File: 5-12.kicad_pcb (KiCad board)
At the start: 2 copper layers, 266.7 x 95.2 mm, 136 parts, among them SW1 SW_Push, U1 ATmega32U4-AU, Y1 16MHz

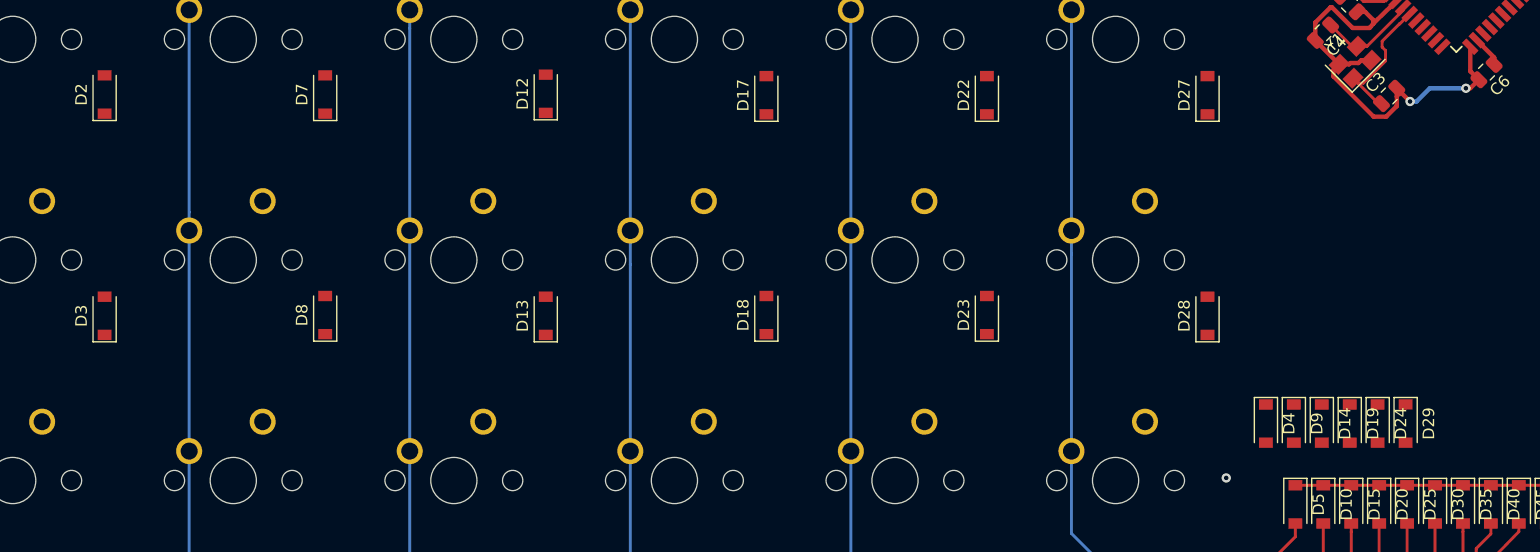
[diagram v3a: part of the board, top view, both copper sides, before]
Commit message: Moved left side of R2 into bank, did partial routing from bank back to switches to test the fit
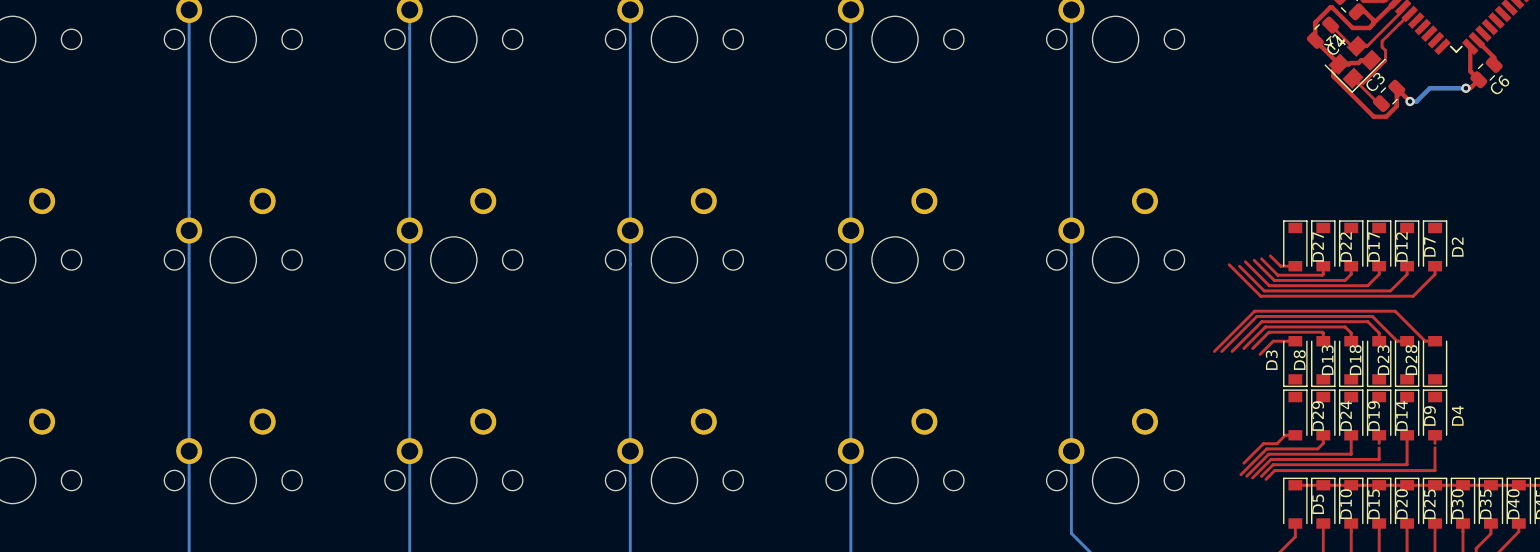
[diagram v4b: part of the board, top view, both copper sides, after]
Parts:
- moved D2 115.7 mm to (144.3, 115.6), turned to 270 degrees
- moved D3 102.9 mm to (132.2, 125.3)
- moved D7 94.4 mm to (141.9, 115.6), turned to 270 degrees
- moved D8 86.3 mm to (134.6, 125.3)
- moved D12 73.2 mm to (139.4, 115.6), turned to 270 degrees
- moved D13 69.7 mm to (137.0, 125.3)
- moved D18 53.1 mm to (139.4, 125.3)
- moved D17 52.2 mm to (137.0, 115.6), turned to 270 degrees
- moved D23 36.5 mm to (141.9, 125.3)
- moved D22 31.9 mm to (134.6, 115.6), turned to 270 degrees
- moved D28 20.0 mm to (144.3, 125.3)
- moved D27 15.2 mm to (132.2, 115.6), turned to 270 degrees
- moved D4 14.6 mm to (144.3, 130.2)
- moved D9 9.80 mm to (141.9, 130.2)
- moved D29 9.55 mm to (132.2, 130.2)
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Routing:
- net Net-(D28-Pad2): track 0.00 -> 21.6 mm
- net Net-(D2-Pad2): track 0.00 -> 20.4 mm
- net Net-(D23-Pad2): track 0.00 -> 18.1 mm
- net Net-(D4-Pad2): track 0.00 -> 17.6 mm
- net Net-(D7-Pad2): track 0.00 -> 16.7 mm
- net Net-(D9-Pad2): track 0.00 -> 15.2 mm
- net Net-(D18-Pad2): track 0.00 -> 14.9 mm
- net Net-(D12-Pad2): track 0.00 -> 13.5 mm
- net Net-(D14-Pad2): track 0.00 -> 13.3 mm
- net Net-(D19-Pad2): track 0.00 -> 11.4 mm
- net Net-(D13-Pad2): track 0.00 -> 11.0 mm
- net Net-(D17-Pad2): track 0.00 -> 10.0 mm
- net Net-(D24-Pad2): track 0.00 -> 8.93 mm
- net Net-(D8-Pad2): track 0.00 -> 7.41 mm
- net Net-(D22-Pad2): track 0.00 -> 6.65 mm
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
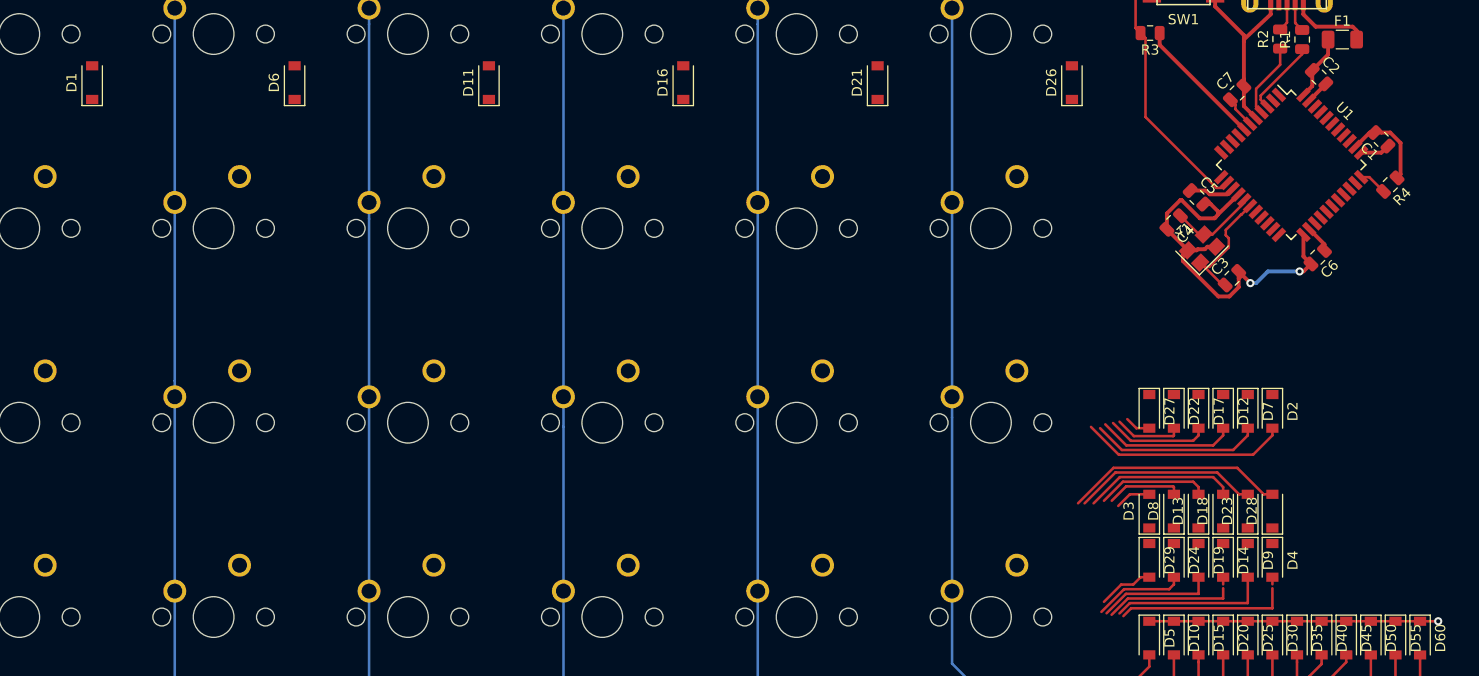
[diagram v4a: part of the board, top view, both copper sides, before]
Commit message: finished left diode banks and their initial routes
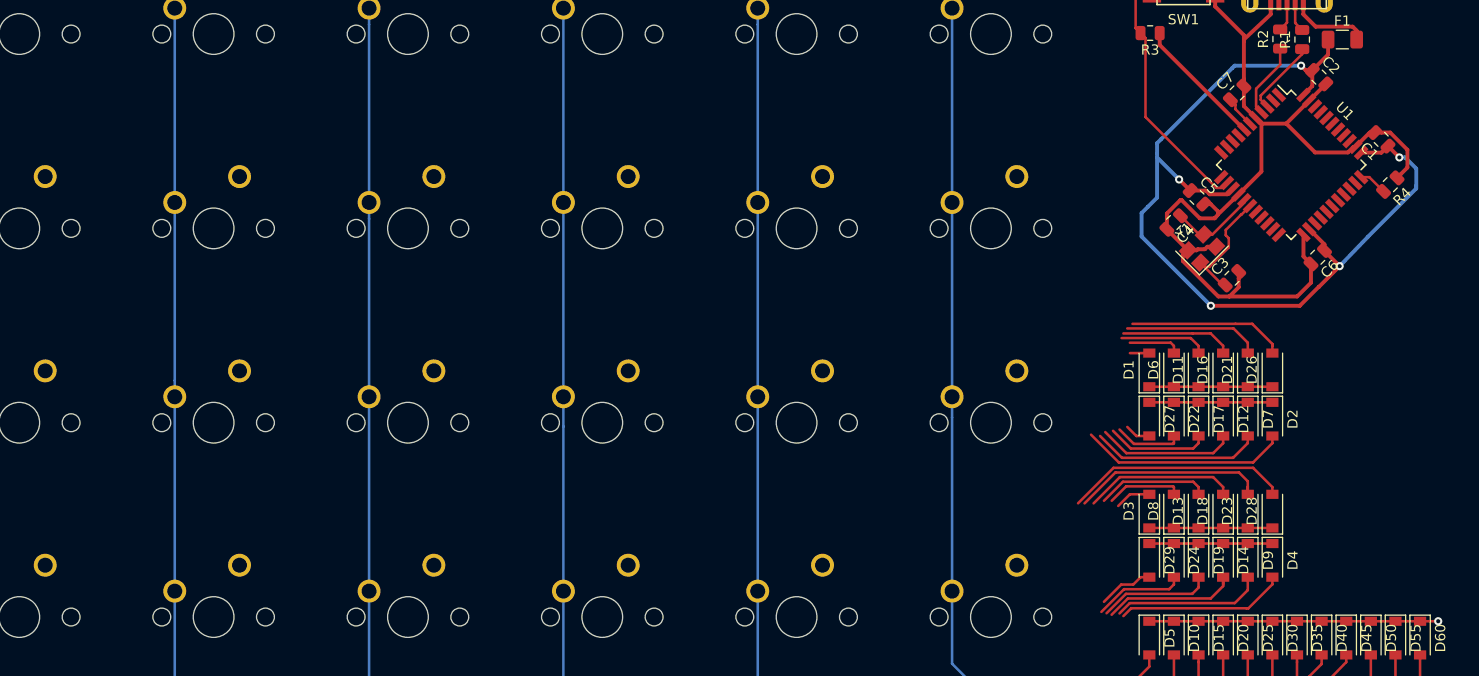
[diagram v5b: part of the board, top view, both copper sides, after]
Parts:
- moved D1 107.4 mm to (132.2, 111.5)
- moved D6 90.7 mm to (134.6, 111.5)
- moved D11 75.0 mm to (137.0, 111.5)
- moved D16 60.0 mm to (139.4, 111.5)
- moved D21 45.9 mm to (141.9, 111.5)
- moved D26 34.3 mm to (144.3, 111.5)
- moved D12 0.76 mm to (139.4, 116.3)
- moved D17 0.76 mm to (137.0, 116.3)
- moved D2 0.76 mm to (144.3, 116.3)
- moved D22 0.76 mm to (134.6, 116.3)
- moved D27 0.76 mm to (132.2, 116.3)
- moved D7 0.76 mm to (141.9, 116.3)
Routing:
- net +5V: track 29.5 -> 104.8 mm, vias 0 -> 5
- net GND: track 71.2 -> 96.7 mm, vias 2 -> 0
- net Net-(D26-Pad2): track 0.00 -> 15.4 mm
- net Net-(D21-Pad2): track 0.00 -> 13.4 mm
- net Row3: track 0.00 -> 12.1 mm
- net Row1: track 0.00 -> 12.1 mm
- net Row2: track 0.00 -> 12.1 mm
- net Row0: track 0.00 -> 12.1 mm
- net Net-(D16-Pad2): track 0.00 -> 11.0 mm
- net Net-(D11-Pad2): track 0.00 -> 8.57 mm
- net Net-(D6-Pad2): track 0.00 -> 5.15 mm
- net Net-(D1-Pad2): track 0.00 -> 1.90 mm
- net Net-(D23-Pad2): track 18.1 -> 19.1 mm
- net Net-(D4-Pad2): track 17.6 -> 16.6 mm
- net Net-(D9-Pad2): track 15.2 -> 14.4 mm

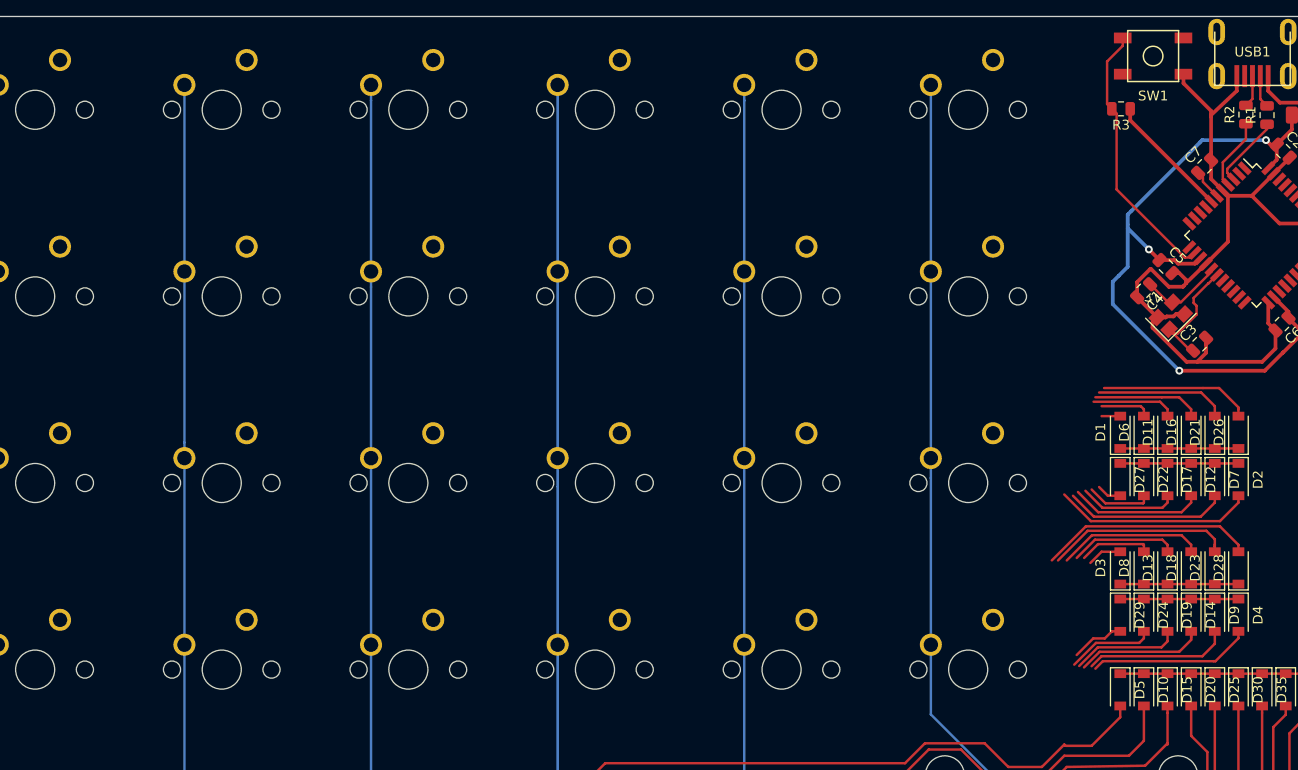
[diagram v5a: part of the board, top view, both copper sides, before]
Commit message: Finished initial routing of left switches to left diode banks
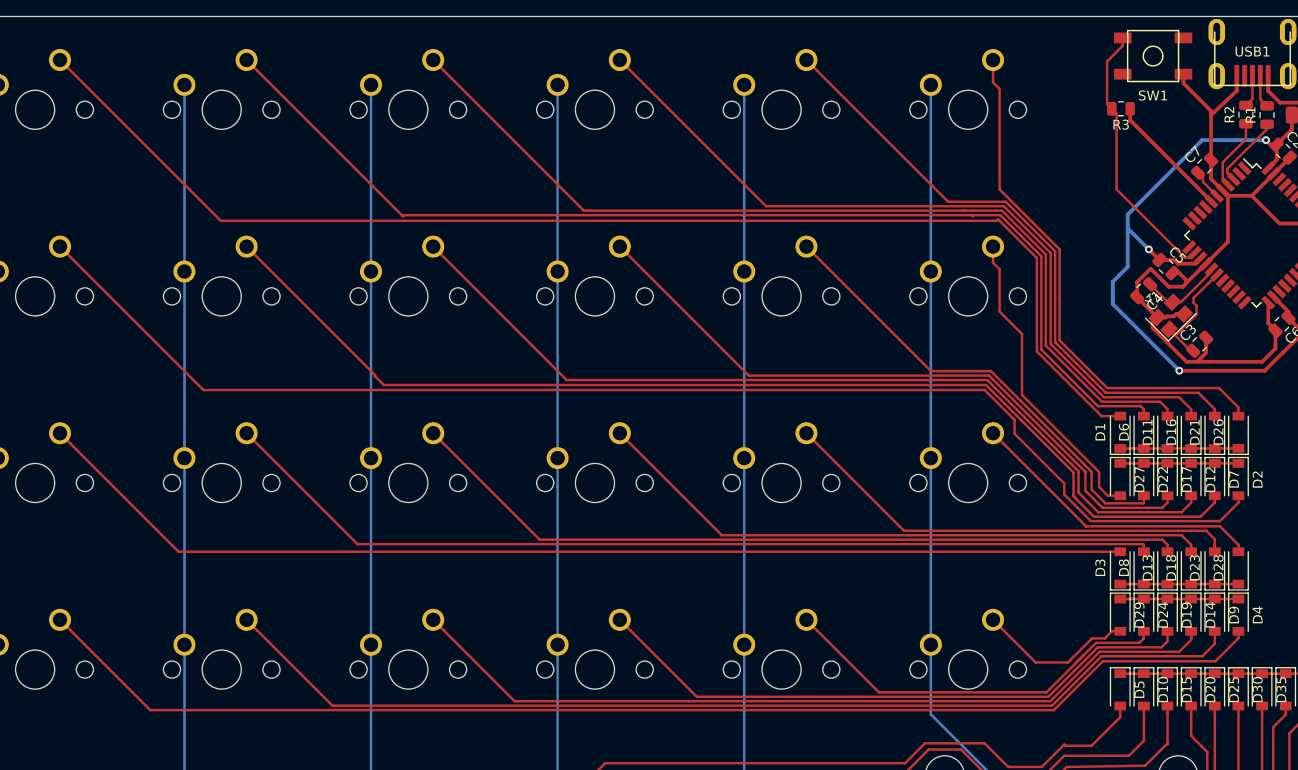
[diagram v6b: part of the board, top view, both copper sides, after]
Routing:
- net Net-(D1-Pad2): track 1.90 -> 129.0 mm
- net Net-(D2-Pad2): track 20.4 -> 134.9 mm
- net Net-(D4-Pad2): track 16.6 -> 127.9 mm
- net Net-(D3-Pad2): track 3.52 -> 113.2 mm
- net Net-(D6-Pad2): track 5.15 -> 112.9 mm
- net Net-(D7-Pad2): track 16.7 -> 113.4 mm
- net Net-(D9-Pad2): track 14.4 -> 106.0 mm
- net Net-(D8-Pad2): track 7.41 -> 97.0 mm
- net Net-(D11-Pad2): track 8.57 -> 96.1 mm
- net Net-(D12-Pad2): track 13.5 -> 91.1 mm
- net Net-(D14-Pad2): track 13.7 -> 85.0 mm
- net Net-(D13-Pad2): track 11.0 -> 80.4 mm
- net Net-(D16-Pad2): track 11.0 -> 79.2 mm
- net Net-(D17-Pad2): track 10.0 -> 69.0 mm
- net Net-(D19-Pad2): track 11.1 -> 62.5 mm
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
